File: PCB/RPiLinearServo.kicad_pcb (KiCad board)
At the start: 2 copper layers, 42.2 x 30.2 mm, 15 parts, among them J1 Conn_01x03_Pin, J2 Conn_02x02_Odd_Even, U1 TMC2209_SILENTSTEPSTICK, U2 RP2040-ZERO, U3 DRV5055A3xDBZxQ1

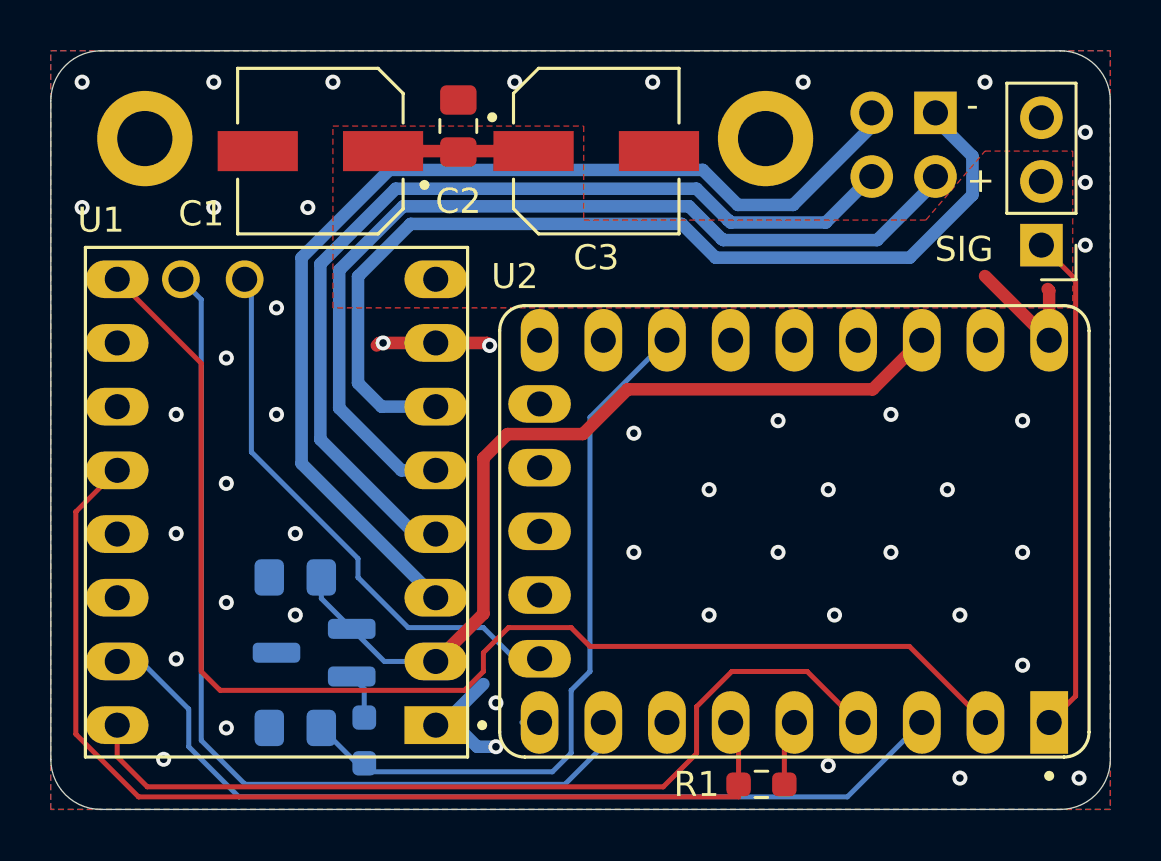
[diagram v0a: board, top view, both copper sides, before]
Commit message: Add ESD protection on pwm input, fix wrapping bug in nvm storage logic
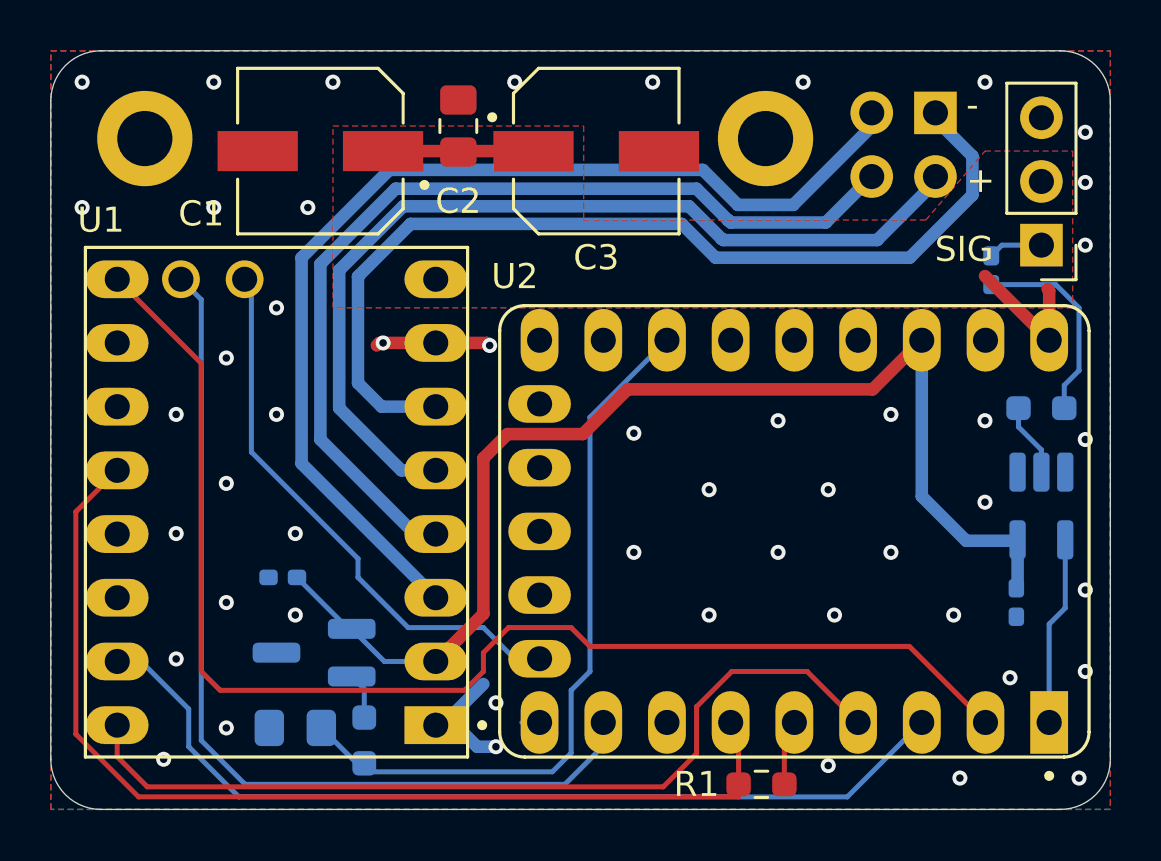
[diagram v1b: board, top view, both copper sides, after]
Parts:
- added C6: 0.1uF, Capacitor_SMD:C_0402_1005Metric_Pad0.74x0.62mm_HandSolder, B.Cu at (164.8, 98.0)
- added D1: TPD1E10B06DPYR, Diode_SMD:D_0402_1005Metric_Pad0.77x0.64mm_HandSolder, B.Cu at (163.8, 84.8)
- added R3: 330, Resistor_SMD:R_0603_1608Metric_Pad0.98x0.95mm_HandSolder, B.Cu at (165.8, 90.2)
- added U4: 74LVC1G17, Package_TO_SOT_SMD:SOT-23-5_HandSoldering, B.Cu at (165.8, 94.2)
- C4: value 2.2uF -> 0.1uF; footprint Capacitor_SMD:C_0805_2012Metric_Pad1.18x1.45mm_HandSolder -> Capacitor_SMD:C_0402_1005Metric_Pad0.74x0.62mm_HandSolder
- moved C4 0.50 mm to (135.5, 97.0)
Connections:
- J1 pad 1: PWM_INPUT -> PWM_UNFILTERED
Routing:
- net +3V3: track 35.2 -> 48.3 mm
- net PWM_INPUT: track 20.0 -> 7.45 mm
- net Net-(D1-Pad2): track 0.00 -> 8.13 mm
- net Net-(R3-Pad2): track 0.00 -> 3.03 mm
- net PWM_UNFILTERED: track 0.00 -> 2.18 mm
- net GND: vias 47 -> 49

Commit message: Update Layout and BOM with minor routing and footprint changes for PWM input voltage protection
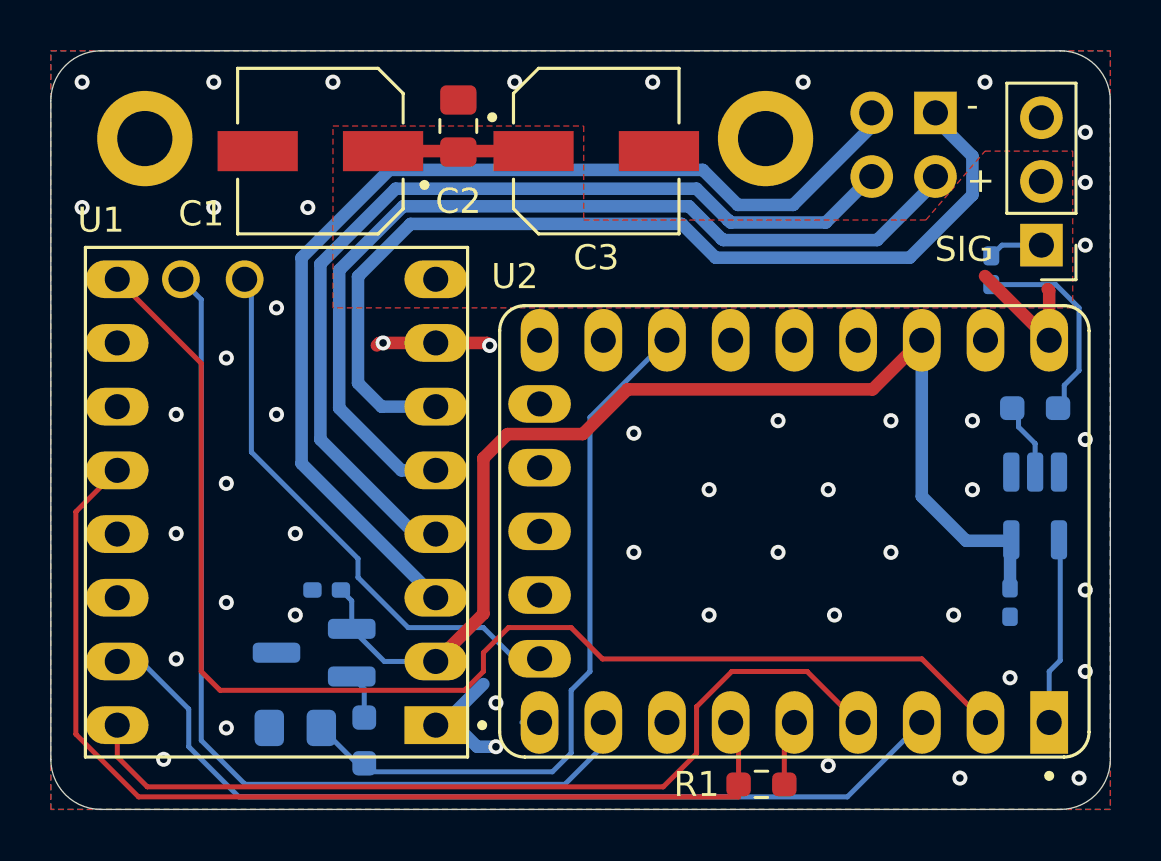
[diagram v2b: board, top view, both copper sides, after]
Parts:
- moved C4 1.82 mm to (137.2, 97.5)
- moved C6 0.25 mm to (164.5, 98.0)
- moved R3 0.25 mm to (165.5, 90.2)
- moved U4 0.25 mm to (165.5, 94.2)
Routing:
- net +3V3: track 48.3 -> 46.4 mm
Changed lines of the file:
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@@
 	(footprint "Capacitor_SMD:C_0402_1005Metric_Pad0.74x0.62mm_HandSolder"
 		(layer "B.Cu")
-		(at 135.5 97 180)
+		(at 137.25 97.5 180)
 		(descr "Capacitor SMD 0402 (1005 Metric), square (rectangular) end terminal, IPC-7351 nominal with elongated pad for handsoldering. (Body size source: IPC-SM-782 page 76, https://www.pcb-3d.com/wordpress/wp-content/uploads/ipc-sm-782a_amendment_1_and_2.pdf), generated with kicad-footprint-generator")
 		(tags "capacitor handsolder")
 		(property "Reference" "C4"
-			(at 0 1.16 0)
+			(at 2.25 0 0)
 			(layer "B.SilkS")
 			(effects
@@
 			(at 0 -1.16 0)
 			(layer "B.Fab")
+			(hide yes)
 			(effects
 				(font
@@
 	(footprint "Package_TO_SOT_SMD:SOT-23-5_HandSoldering"
 		(layer "B.Cu")
-		(at 165.75 94.15 -90)
+		(at 165.5 94.15 -90)
 		(descr "5-pin SOT23 package")
 		(tags "SOT-23-5 hand-soldering")
 		(property "Reference" "U4"
-			(at 3.25 -1 180)
+			(at -1.9 2.75 180)
 			(layer "B.SilkS")
 			(effects
@@
 	(footprint "Capacitor_SMD:C_0402_1005Metric_Pad0.74x0.62mm_HandSolder"
 		(layer "B.Cu")
-		(at 164.75 98 -90)
+		(at 164.5 98 -90)
 		(descr "Capacitor SMD 0402 (1005 Metric), square (rectangular) end terminal, IPC-7351 nominal with elongated pad for handsoldering. (Body size source: IPC-SM-782 page 76, https://www.pcb-3d.com/wordpress/wp-content/uploads/ipc-sm-782a_amendment_1_and_2.pdf), generated with kicad-footprint-generator")
 		(tags "capacitor handsolder")
@@
 	(footprint "Resistor_SMD:R_0603_1608Metric_Pad0.98x0.95mm_HandSolder"
 		(layer "B.Cu")
-		(at 165.75 90.25 180)
+		(at 165.5 90.25 180)
 		(descr "Resistor SMD 0603 (1608 Metric), square (rectangular) end terminal, IPC-7351 nominal with elongated pad for handsoldering. (Body size source: IPC-SM-782 page 72, https://www.pcb-3d.com/wordpress/wp-content/uploads/ipc-sm-782a_amendment_1_and_2.pdf), generated with kicad-footprint-generator")
 		(tags "resistor handsolder")
@@
 	)
 	(via
-		(at 159.75 90.5)
+		(at 159.75 90.75)
 		(size 0.6)
 		(drill 0.3)
@@
 	)
 	(via
-		(at 163.5 94)
-		(size 0.6)
-		(drill 0.3)
-		(layers "F.Cu" "B.Cu")
-		(free yes)
-		(net 1)
-	)
-	(via
-		(at 163.5 90.75)
+		(at 163 93.5)
+		(size 0.6)
+		(drill 0.3)
+		(layers "F.Cu" "B.Cu")
+		(free yes)
+		(net 1)
+	)
+	(via
+		(at 163 90.75)
 		(size 0.6)
 		(drill 0.3)
@@
 	)
 	(segment
-		(start 166.06 98.86)
+		(start 166.5 100.31)
+		(end 166.06 100.75)
+		(width 0.2)
+		(layer "B.Cu")
+		(net 3)
+	)
+	(segment
+		(start 166.5 95.8)
+		(end 166.5 100.31)
+		(width 0.2)
+		(layer "B.Cu")
+		(net 3)
+	)
+	(segment
+		(start 166.06 100.75)
 		(end 166.06 102.7825)
-		(width 0.2)
-		(layer "B.Cu")
-		(net 3)
-	)
-	(segment
-		(start 166.7 95.6)
-		(end 166.7 98.22)
-		(width 0.2)
-		(layer "B.Cu")
-		(net 3)
-	)
-	(segment
-		(start 166.7 98.22)
-		(end 166.06 98.86)
 		(width 0.2)
 		(layer "B.Cu")
@@
 	)
 	(segment
+		(start 128.9 85.11)
+		(end 132.25 88.46)
+		(width 0.2)
+		(layer "F.Cu")
+		(net 13)
+	)
+	(segment
 		(start 143.5 100)
 		(end 144.5 99)
@@
 	)
 	(segment
-		(start 128.9 85.11)
-		(end 132.25 88.46)
+		(start 133 101.5)
+		(end 142.75 101.5)
+		(width 0.2)
+		(layer "F.Cu")
+		(net 13)
+	)
+	(segment
+		(start 142.75 101.5)
+		(end 143.5 100.75)
 		(width 0.2)
 		(layer "F.Cu")
@@
 	)
 	(segment
-		(start 133 101.5)
-		(end 142.75 101.5)
-		(width 0.2)
-		(layer "F.Cu")
-		(net 13)
-	)
-	(segment
-		(start 147.75 99.75)
-		(end 160.4875 99.75)
-		(width 0.2)
-		(layer "F.Cu")
-		(net 13)
-	)
-	(segment
-		(start 160.4875 99.75)
-		(end 163.52 102.7825)
-		(width 0.2)
-		(layer "F.Cu")
-		(net 13)
-	)
-	(segment
-		(start 147 99)
-		(end 147.75 99.75)
+		(start 148.25 100.25)
+		(end 160.9875 100.25)
 		(width 0.2)
 		(layer "F.Cu")
@@
 	)
 	(segment
-		(start 142.75 101.5)
-		(end 143.5 100.75)
+		(start 160.9875 100.25)
+		(end 163.52 102.7825)
+		(width 0.2)
+		(layer "F.Cu")
+		(net 13)
+	)
+	(segment
+		(start 147 99)
+		(end 148.25 100.25)
 		(width 0.2)
 		(layer "F.Cu")
@@
 	)
 	(segment
-		(start 136.0675 97)
-		(end 138.1175 99.05)
-		(width 0.2)
+		(start 162.75 95.5375)
+		(end 164.5125 95.5375)
+		(width 0.5)
+		(layer "B.Cu")
+		(net 15)
+	)
+	(segment
+		(start 160.98 87.5425)
+		(end 160.98 93.7675)
+		(width 0.5)
 		(layer "B.Cu")
 		(net 15)
@@
 	)
 	(segment
+		(start 164.5 95.775)
+		(end 164.5 97.1125)
+		(width 0.5)
+		(layer "B.Cu")
+		(net 15)
+	)
+	(segment
 		(start 160.98 93.7675)
 		(end 162.75 95.5375)
@@
 	)
 	(segment
-		(start 164.7375 95.5375)
-		(end 164.8 95.6)
-		(width 0.5)
+		(start 138.25 99.05)
+		(end 138.25 97.9325)
+		(width 0.2)
 		(layer "B.Cu")
 		(net 15)
 	)
 	(segment
-		(start 164.8 95.6)
-		(end 164.8 97.4125)
-		(width 0.5)
+		(start 138.25 97.9325)
+		(end 137.8175 97.5)
+		(width 0.2)
 		(layer "B.Cu")
 		(net 15)
@@
 	)
 	(segment
-		(start 160.98 87.5425)
-		(end 160.98 93.7675)
-		(width 0.5)
-		(layer "B.Cu")
-		(net 15)
-	)
-	(segment
-		(start 162.75 95.5375)
-		(end 164.7375 95.5375)
+		(start 164.5125 95.5375)
+		(end 164.55 95.5)
 		(width 0.5)
 		(layer "B.Cu")
@@
 	)
 	(segment
-		(start 165.75 91.9125)
-		(end 165.75 92.9)
+		(start 164.8375 91)
+		(end 165.5 91.6625)
 		(width 0.2)
 		(layer "B.Cu")
@@
 	)
 	(segment
-		(start 164.8375 91)
-		(end 165.75 91.9125)
-		(width 0.2)
-		(layer "B.Cu")
+		(start 165.5 91.6625)
+		(end 165.5 92.8)
+		(width 0.2)
+		(layer "B.Cu")
+		(net 33)
+	)
+	(segment
+		(start 165.5 92.8)
+		(end 165.6 92.9)
+		(width 0.2)
+		(layer "B.Cu")
